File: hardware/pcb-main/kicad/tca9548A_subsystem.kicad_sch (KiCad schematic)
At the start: 6 parts, among them U4 TCA9548APWR

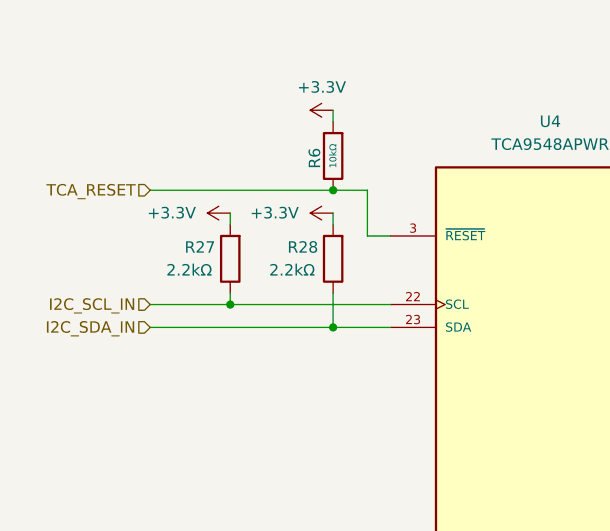
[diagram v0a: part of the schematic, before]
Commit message: Updated to use ultra simplified 3v buck converter
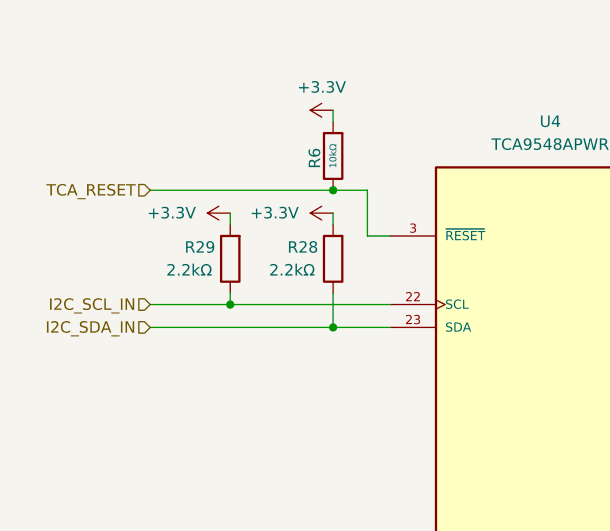
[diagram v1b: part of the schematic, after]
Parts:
- renumbered R27 to R29
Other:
- title: (none) -> Motion Play Main Board
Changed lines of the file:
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@@
 	(generator_version "9.0")
 	(paper "A4")
+	(title_block
+		(title "Motion Play Main Board")
+		(date "2025-09-07")
+		(rev "5.0")
+	)
 	(junction
 		(at 128.27 71.12)
@@
 		(on_board yes)
 		(dnp no)
-		(property "Reference" "R27"
+		(property "Reference" "R29"
 			(at 123.19 64.77 0)
 			(effects
@@
 			(project ""
 				(path "/6e095bf3-d8d5-4f67-b79f-a2965409c7a9/bfeba651-d961-4d9b-b09b-91dbbe05d3fa"
-					(reference "R27")
+					(reference "R29")
 					(unit 1)
 				)
